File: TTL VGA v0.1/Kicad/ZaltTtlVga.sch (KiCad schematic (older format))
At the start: 11 parts, among them U301 74LS393, U302 74LS393, U303 74LS393, X301 ACO-25.175MHz

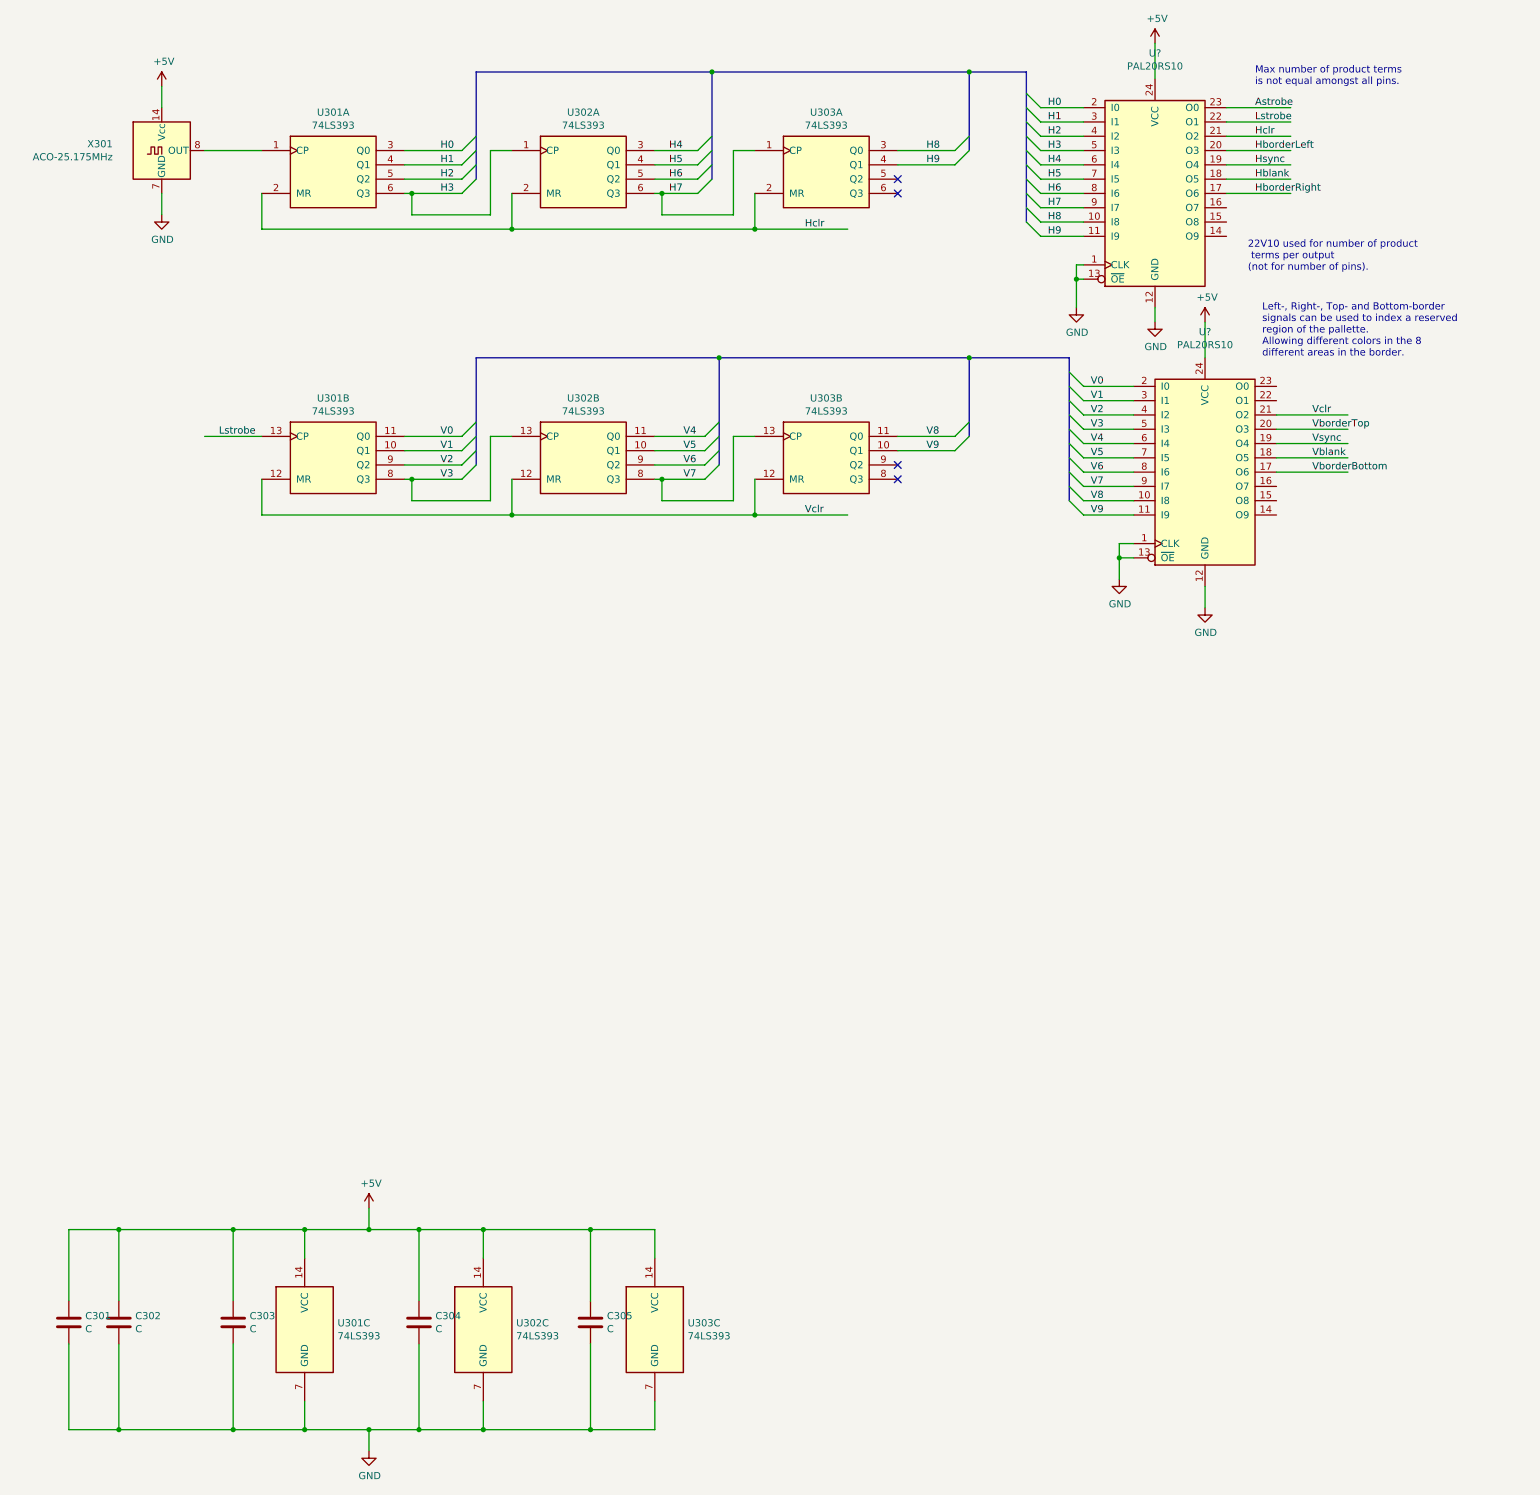
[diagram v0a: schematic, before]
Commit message: more sheets in schematic
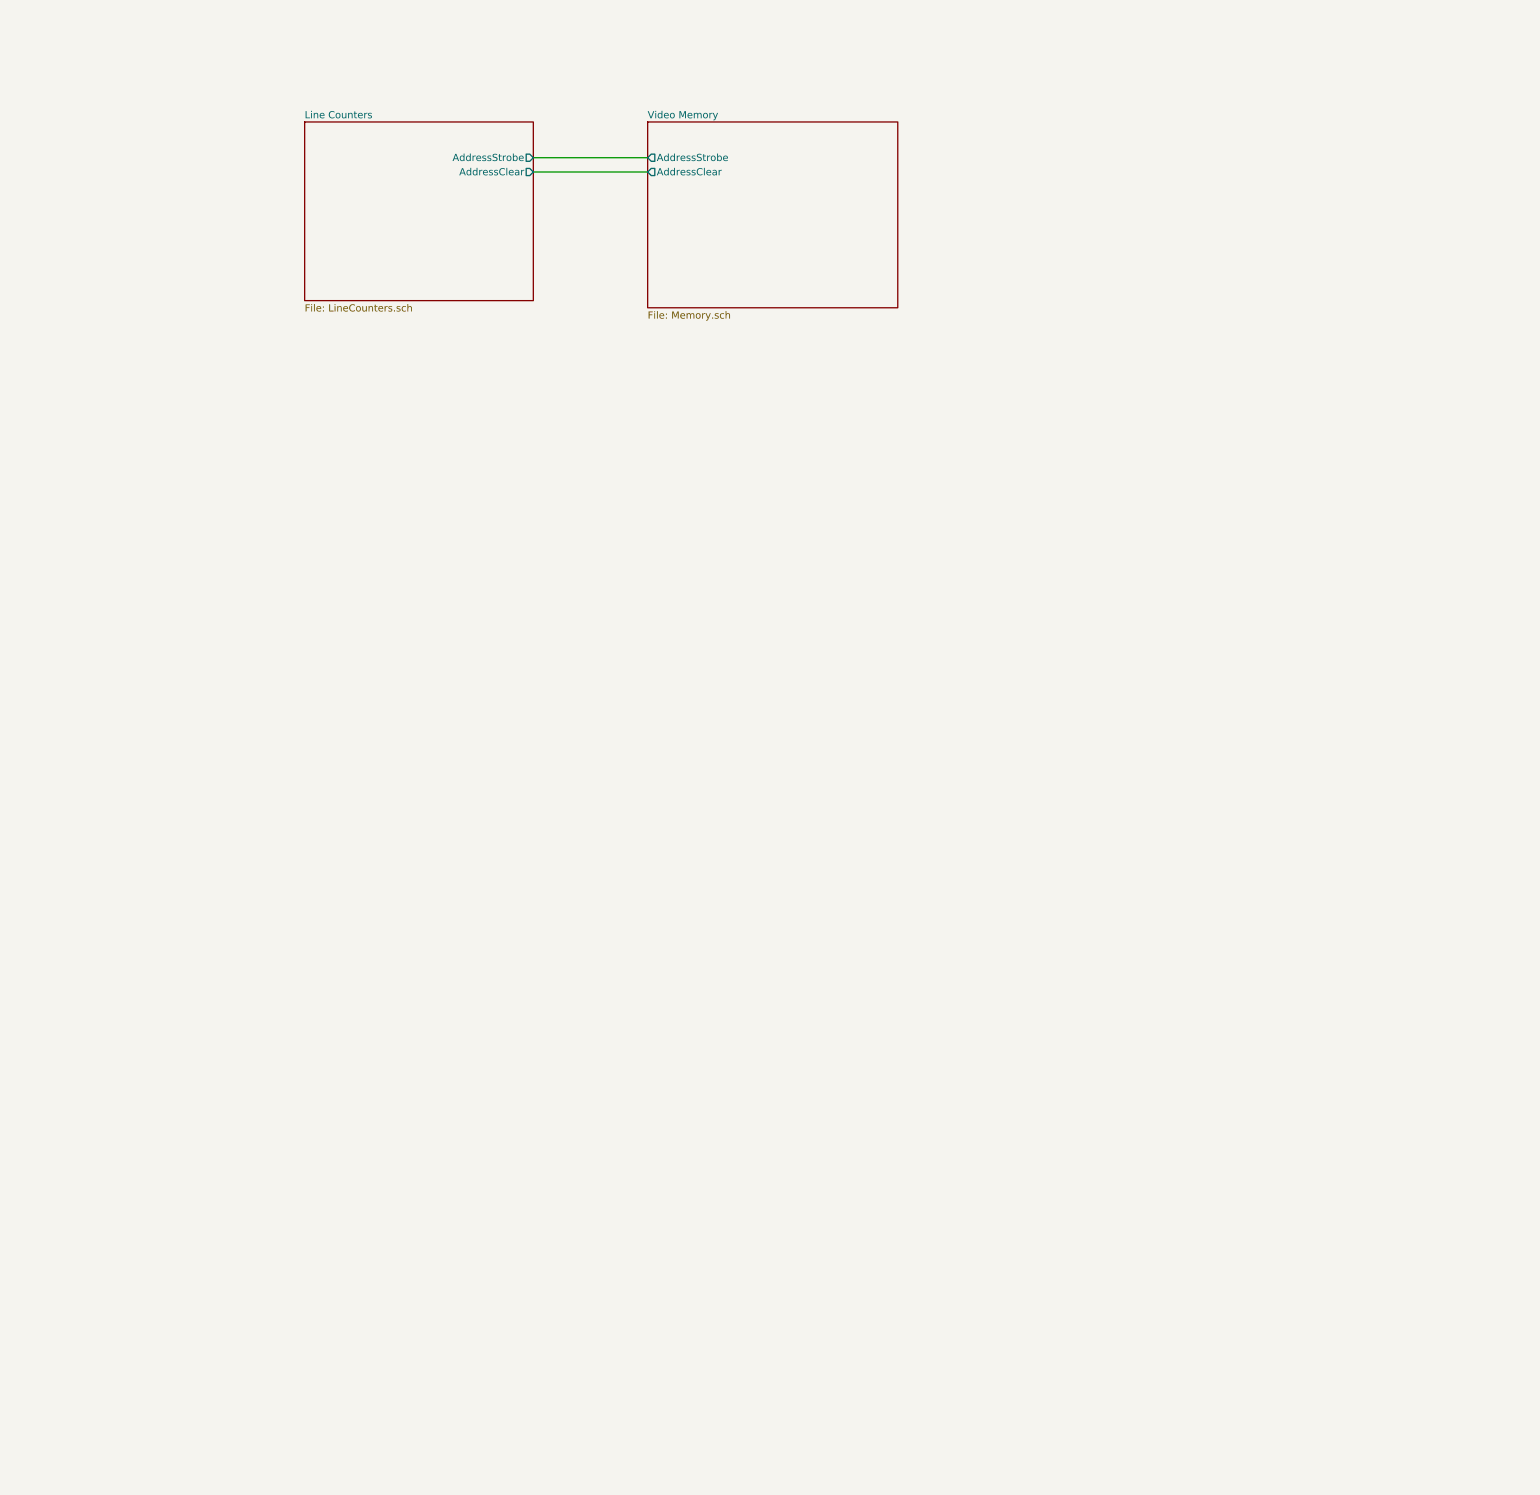
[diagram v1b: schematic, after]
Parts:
- removed C301, C302, C303, C304, C305: C, symbol Device:C
- removed U301, U302, U303: 74LS393, symbol 74xx:74LS393
- removed U? (x2): PAL20RS10, symbol Logic_Programmable:PAL20RS10
- removed X301: ACO-25.175MHz, Oscillator:Oscillator_DIP-14, symbol Oscillator:ACO-xxxMHz
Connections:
- net labels removed: +5V, Astrobe, GND, H0, H1, H2, H3, H4, H5, H6, H7, H8, H9, Hblank, HborderLeft, HborderRight, Hclr, Hsync, Lstrobe, V0, V1, V2, V3, V4, V5, V6, V7, V8, V9, Vblank, VborderBottom, VborderTop, Vclr, Vsync
- wire segments 134 -> 2
- no-connect marks 4 -> 0
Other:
- note removed: "22V10 used for number of product\n terms per output \n(not for number of pins)."
- note removed: "Left-, Right-, Top- and Bottom-border \nsignals can be used to index a reserved \nregion of the pallette.\nAllowing different colors in the 8 \ndifferent areas in the border."
- note removed: "Max number of product terms\nis not equal amongst all pins."

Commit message: tweaks
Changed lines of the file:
@@
 $Descr A4 11693 8268
 encoding utf-8
-Sheet 1 3
+Sheet 1 5
 Title "Zalt TTL VGA"
 Date "2020-02-09"
@@
 Comment1 "640x480 @60Hz"
 Comment2 "512x384 + border"
-Comment3 ""
+Comment3 "Video Memory"
 Comment4 ""
 $EndDescr
 $Sheet
-S 2700 1500 1600 1250
+S 3250 1500 1050 1250
 U 5E451FD0
 F0 "Line Counters" 50
@@
 F2 "AddressStrobe" O R 4300 1750 50
 F3 "AddressClear" O R 4300 1850 50
+F4 "~AddressEnable" O R 4300 1950 50
 $EndSheet
 $Sheet
-S 5100 1500 1750 1300
+S 5100 1500 1300 1250
 U 5E4A1CB2
 F0 "Video Memory" 50
 F1 "Memory.sch" 50
-F2 "AddressStrobe" O L 5100 1750 50
-F3 "AddressClear" O L 5100 1850 50
+F2 "AddressStrobe" I L 5100 1750 50
+F3 "AddressClear" I L 5100 1850 50
+F4 "~AddressEnable" I L 5100 1950 50
+F5 "BusAddress" I L 5100 2300 50
+F6 "BusData" I L 5100 2400 50
+F7 "BusControl" I L 5100 2500 50
+F8 "PixelData" I R 6400 1750 50
 $EndSheet
 Wire Wire Line
@@
 Wire Wire Line
 	4300 1850 5100 1850
+Wire Wire Line
+	4300 1950 5100 1950
+$Sheet
+S 6900 1500 1100 1250
+U 5E4F03C9
+F0 "Pixel Output" 50
+F1 "PixelOutput.sch" 50
+F2 "PixelData" I L 6900 1750 50
+$EndSheet
+Wire Bus Line
+	6400 1750 6900 1750
 $EndSCHEMATC

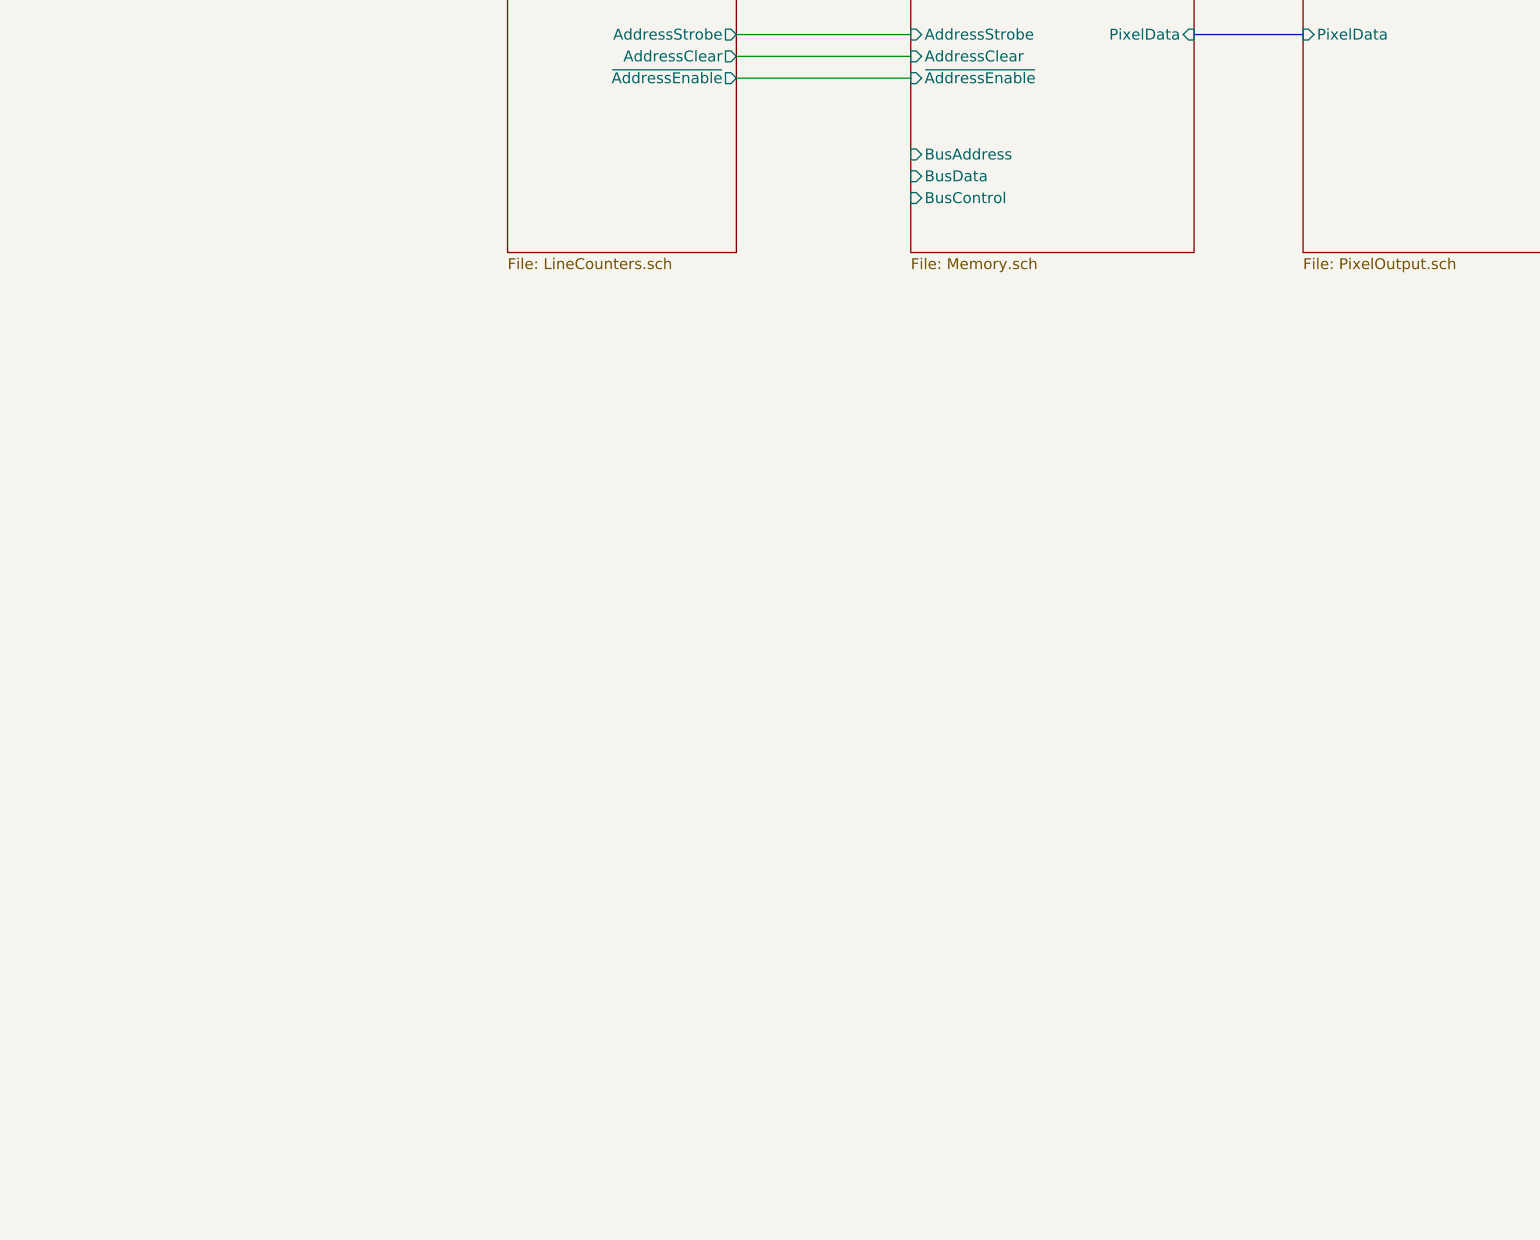
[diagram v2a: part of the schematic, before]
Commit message: vga memory interface
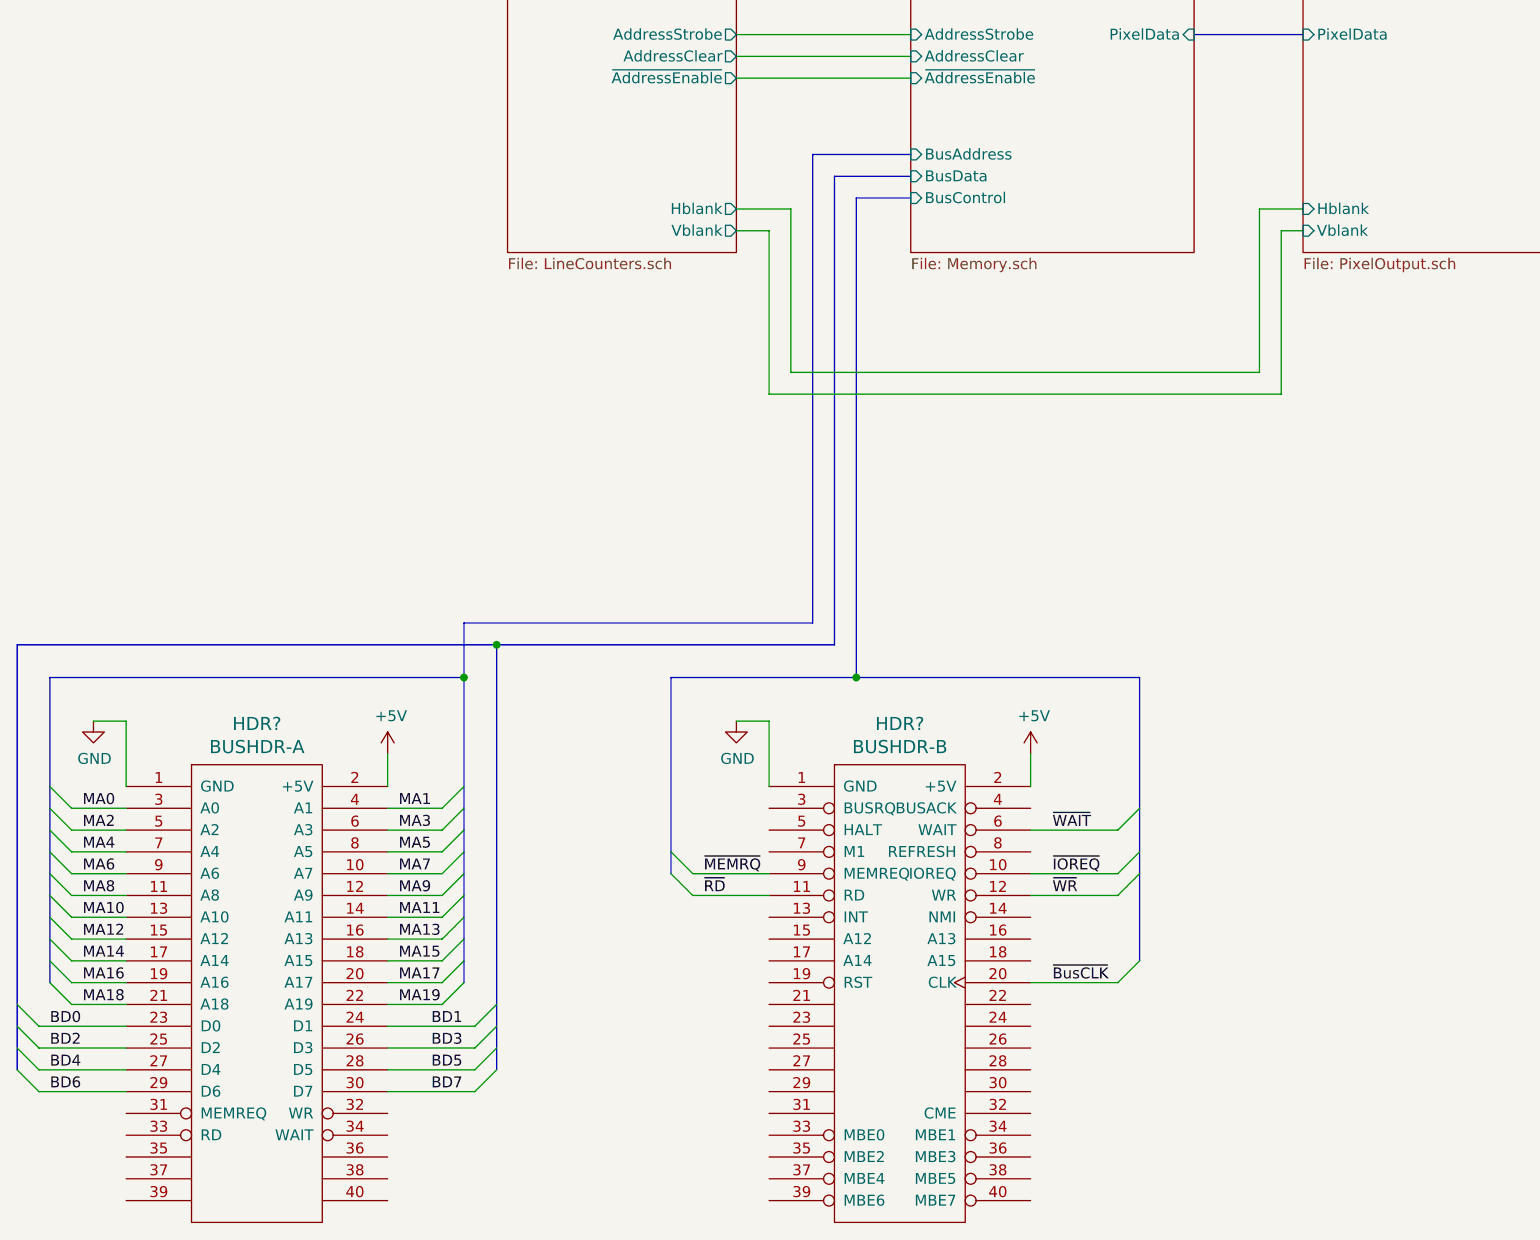
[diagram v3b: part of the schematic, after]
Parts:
- added HDR?: BUSHDR-A, symbol syshdr:BUSHDR-A
- added HDR?: BUSHDR-B, symbol syshdr:BUSHDR-B
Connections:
- new net +5V: HDR?.2 (+5V), HDR?.2 (+5V)
- new net BD0: HDR?.23 (D0)
- new net BD1: HDR?.24 (D1)
- new net BD2: HDR?.25 (D2)
- new net BD3: HDR?.26 (D3)
- new net BD4: HDR?.27 (D4)
- new net BD5: HDR?.28 (D5)
- new net BD6: HDR?.29 (D6)
- new net BD7: HDR?.30 (D7)
- new net GND: HDR?.1 (GND), HDR?.1 (GND)
- new net MA0: HDR?.3 (A0)
- new net MA1: HDR?.4 (A1)
- new net MA10: HDR?.13 (A10)
- new net MA11: HDR?.14 (A11)
- new net MA12: HDR?.15 (A12)
- new net MA13: HDR?.16 (A13)
- new net MA14: HDR?.17 (A14)
- new net MA15: HDR?.18 (A15)
- new net MA16: HDR?.19 (A16)
- new net MA17: HDR?.20 (A17)
- new net MA18: HDR?.21 (A18)
- new net MA19: HDR?.22 (A19)
- new net MA2: HDR?.5 (A2)
- new net MA3: HDR?.6 (A3)
- new net MA4: HDR?.7 (A4)
- new net MA5: HDR?.8 (A5)
- new net MA6: HDR?.9 (A6)
- new net MA7: HDR?.10 (A7)
- new net MA8: HDR?.11 (A8)
- new net MA9: HDR?.12 (A9)
- new net ~BusCLK: HDR?.20 (CLK)
- new net ~IOREQ: HDR?.10 (IOREQ)
- new net ~MEMRQ: HDR?.9 (MEMREQ)
- new net ~RD: HDR?.11 (RD)
- new net ~WAIT: HDR?.6 (WAIT)
- new net ~WR: HDR?.12 (WR)
